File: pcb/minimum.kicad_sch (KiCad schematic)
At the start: 32 parts, among them J1 USB4155-03-C_REVA, J2 Conn_01x02, U1 RP2040, U2 SCD4x, U3 W25Q16JVUXIQ, U4 XCL220, Y1 C2E-12.000-18-1020-X-R

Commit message: routing
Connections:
- net Pi_USB_D-: now reaches R2.1, U1.46 (USB_DM)
- net Pi_USB_D+: now reaches R1.2, U1.47 (USB_DP)
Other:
- moved on the sheet: R1, R2
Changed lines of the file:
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@@
     (stroke (width 0) (type solid) (color 0 0 0 0))
   )
-  (wire (pts (xy 212.09 38.735) (xy 217.805 38.735))
-    (stroke (width 0) (type solid) (color 0 0 0 0))
-  )
-  (wire (pts (xy 212.09 41.275) (xy 217.805 41.275))
+  (wire (pts (xy 212.09 38.735) (xy 222.25 38.735))
+    (stroke (width 0) (type solid) (color 0 0 0 0))
+  )
+  (wire (pts (xy 212.09 41.275) (xy 222.25 41.275))
     (stroke (width 0) (type solid) (color 0 0 0 0))
   )
@@
     (stroke (width 0) (type solid) (color 0 0 0 0))
   )
-  (wire (pts (xy 222.885 38.735) (xy 240.665 38.735))
-    (stroke (width 0) (type solid) (color 0 0 0 0))
-  )
-  (wire (pts (xy 222.885 41.275) (xy 240.665 41.275))
+  (wire (pts (xy 227.33 38.735) (xy 240.665 38.735))
+    (stroke (width 0) (type solid) (color 0 0 0 0))
+  )
+  (wire (pts (xy 227.33 41.275) (xy 240.665 41.275))
     (stroke (width 0) (type solid) (color 0 0 0 0))
   )
@@
   )
   (label "SCL" (at 196.85 216.535 0)
+    (effects (font (size 1 1)) (justify left bottom))
+  )
+  (label "Pi_USB_D+" (at 212.725 38.735 0)
+    (effects (font (size 1 1)) (justify left bottom))
+  )
+  (label "Pi_USB_D-" (at 212.725 41.275 0)
     (effects (font (size 1 1)) (justify left bottom))
   )
@@
     (pin "2")
   )
-  (symbol (lib_id "Device:R_Small") (at 220.345 38.735 270) (unit 1)
-    (in_bom yes) (on_board yes)
-    (property "Reference" "R1" (id 0) (at 224.155 37.2068 90))
-    (property "Value" "27.4" (id 1) (at 220.345 36.8069 90))
-    (property "Footprint" "Resistor_SMD:R_0402_1005Metric" (id 2) (at 220.345 38.735 0)
-      (effects (font (size 1.27 1.27)) hide)
-    )
-    (property "Datasheet" "~" (id 3) (at 220.345 38.735 0)
+  (symbol (lib_id "Device:R_Small") (at 224.79 38.735 270) (unit 1)
+    (in_bom yes) (on_board yes)
+    (property "Reference" "R1" (id 0) (at 228.6 37.2068 90))
+    (property "Value" "27.4" (id 1) (at 224.79 36.8069 90))
+    (property "Footprint" "Resistor_SMD:R_0402_1005Metric" (id 2) (at 224.79 38.735 0)
+      (effects (font (size 1.27 1.27)) hide)
+    )
+    (property "Datasheet" "~" (id 3) (at 224.79 38.735 0)
       (effects (font (size 1.27 1.27)) hide)
     )
@@
     (pin "2")
   )
-  (symbol (lib_id "Device:R_Small") (at 220.345 41.275 90) (unit 1)
-    (in_bom yes) (on_board yes)
-    (property "Reference" "R2" (id 0) (at 224.155 42.2868 90))
-    (property "Value" "27.4" (id 1) (at 220.345 43.1569 90))
-    (property "Footprint" "Resistor_SMD:R_0402_1005Metric" (id 2) (at 220.345 41.275 0)
-      (effects (font (size 1.27 1.27)) hide)
-    )
-    (property "Datasheet" "~" (id 3) (at 220.345 41.275 0)
-      (effects (font (size 1.27 1.27)) hide)
-    )
+  (symbol (lib_id "Device:R_Small") (at 224.79 41.275 90) (unit 1)
+    (in_bom yes) (on_board yes)
+    (property "Reference" "R2" (id 0) (at 228.6 42.2868 90))
+    (property "Value" "27.4" (id 1) (at 224.79 43.1569 90))
+    (property "Footprint" "Resistor_SMD:R_0402_1005Metric" (id 2) (at 224.79 41.275 0)
+      (effects (font (size 1.27 1.27)) hide)
+    )
+    (property "Datasheet" "~" (id 3) (at 224.79 41.275 0)
+      (effects (font (size 1.27 1.27)) hide)
+    )

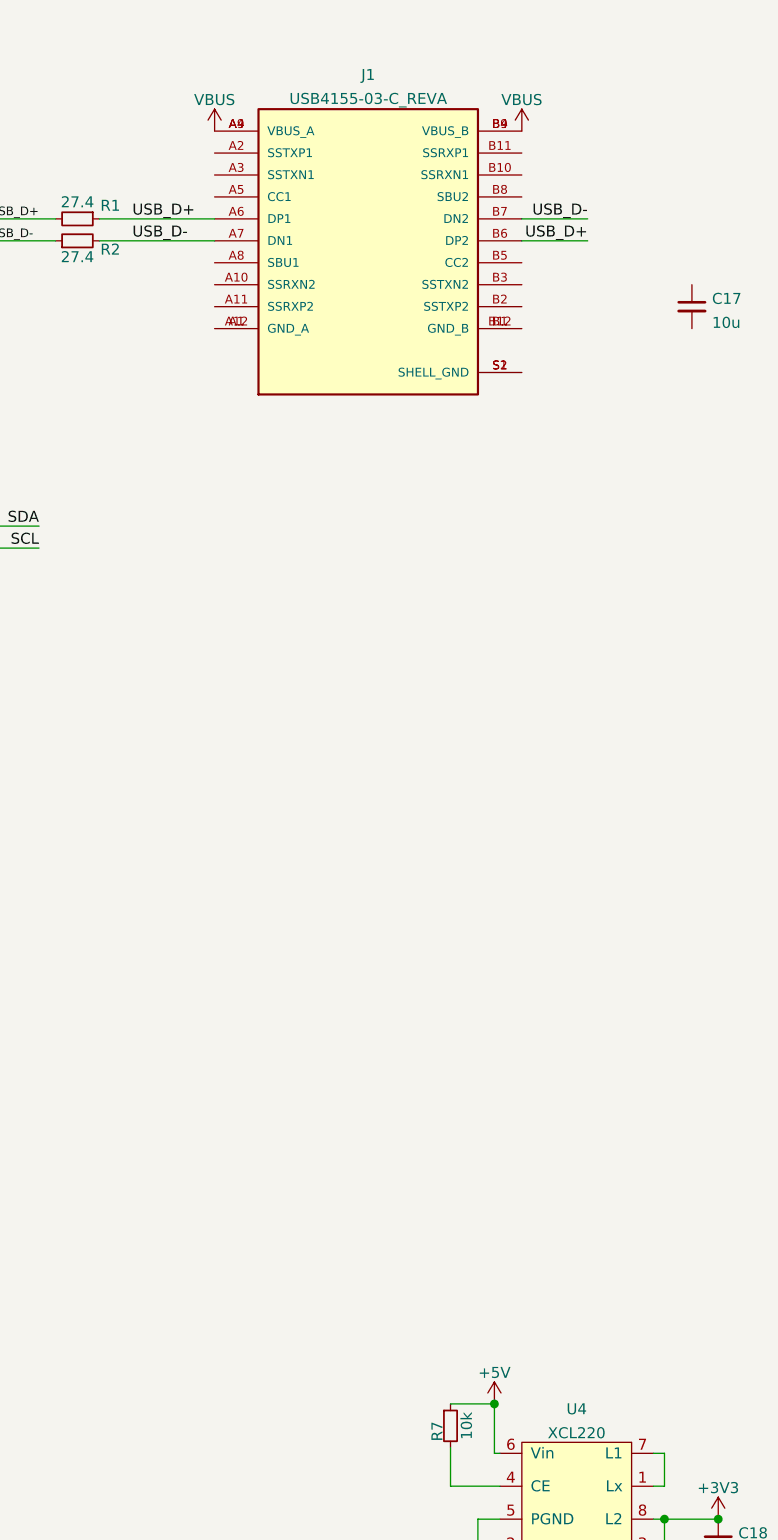
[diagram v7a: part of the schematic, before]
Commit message: routing VBUS
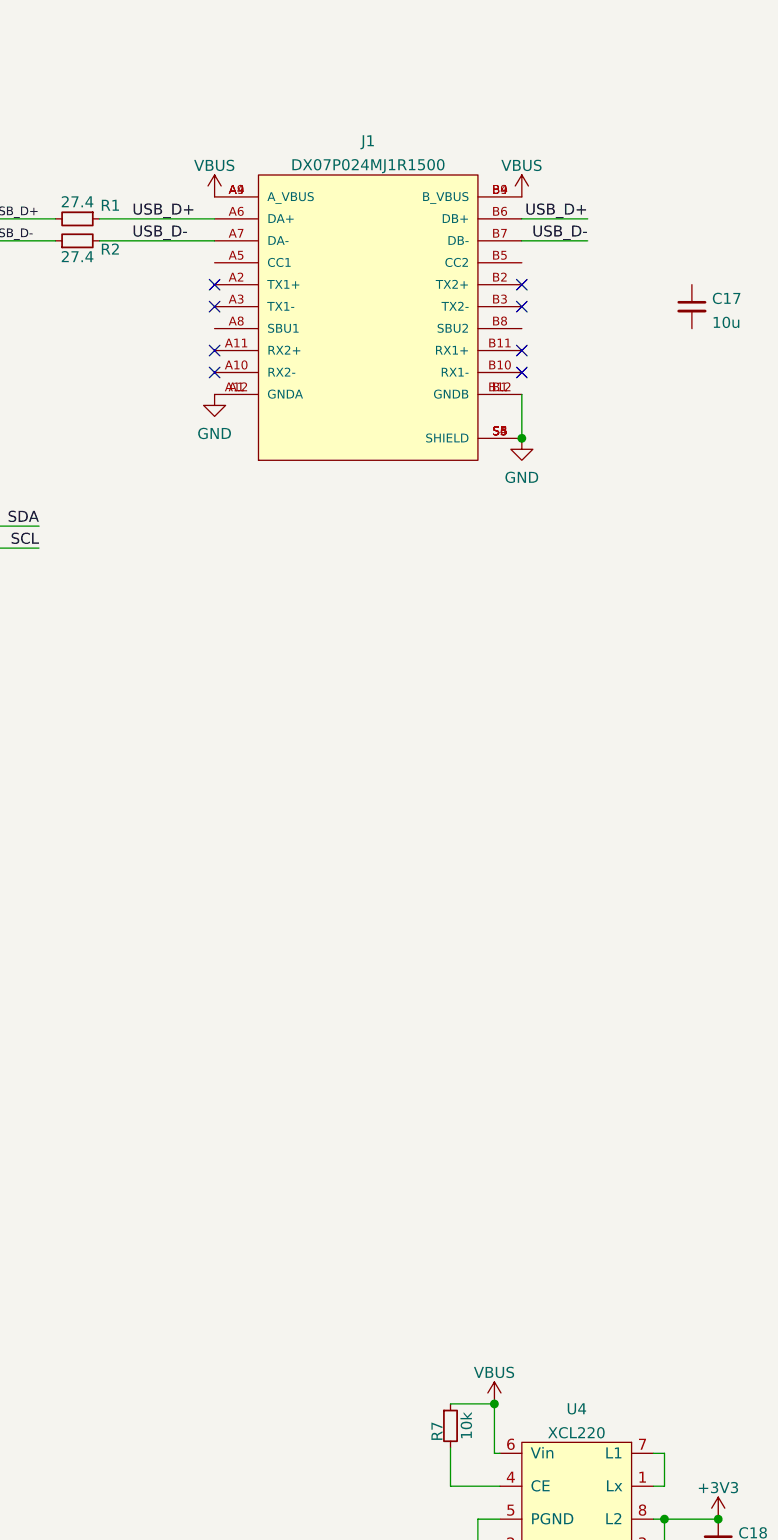
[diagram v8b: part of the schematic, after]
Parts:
- removed J1: USB4155-03-C_REVA, SMD:GCT_USB4155-03-C_REVA, symbol USB4155-03-C_REVA:USB4155-03-C_REVA
- added J1: DX07P024MJ1R1500, SMD:JAE_DX07P024MJ1R1500, symbol DX07P024MJ1R1500:DX07P024MJ1R1500
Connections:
- net +5V is gone; now on net VBUS: R7.1, U4.6 (Vin)
- net GND: now also J1.A1 (GNDA), J1.A12 (GNDA), J1.B1 (GNDB), J1.B12 (GNDB), J1.S3 (SHIELD), J1.S4 (SHIELD), J1.S5 (SHIELD), J1.S6 (SHIELD)
- net USB_D+: now also J1.A6 (DA+), J1.B6 (DB+)
- net USB_D-: now also J1.A7 (DA-), J1.B7 (DB-)
- net VBUS: now also J1.A4 (A_VBUS), J1.A9 (A_VBUS), J1.B4 (B_VBUS), J1.B9 (B_VBUS)
- no-connect marks 0 -> 8
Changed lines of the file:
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@@
   (junction (at 271.145 196.85) (diameter 1.016) (color 0 0 0 0))
   (junction (at 273.05 175.895) (diameter 1.016) (color 0 0 0 0))
+  (junction (at 276.225 64.135) (diameter 1.016) (color 0 0 0 0))
   (junction (at 292.735 189.23) (diameter 1.016) (color 0 0 0 0))
   (junction (at 298.958 189.23) (diameter 1.016) (color 0 0 0 0))
+  (no_connect (at 240.665 46.355))
+  (no_connect (at 240.665 48.895))
+  (no_connect (at 240.665 53.975))
+  (no_connect (at 240.665 56.515))
+  (no_connect (at 276.225 46.355))
+  (no_connect (at 276.225 48.895))
+  (no_connect (at 276.225 53.975))
+  (no_connect (at 276.225 56.515))
   (wire (pts (xy 17.78 45.085) (xy 27.94 45.085))
     (stroke (width 0) (type solid) (color 0 0 0 0))
@@
   )
   (wire (pts (xy 276.225 41.275) (xy 283.845 41.275))
+    (stroke (width 0) (type solid) (color 0 0 0 0))
+  )
+  (wire (pts (xy 276.225 59.055) (xy 276.225 64.135))
     (stroke (width 0) (type solid) (color 0 0 0 0))
   )
@@
     (effects (font (size 1.27 1.27)) (justify left bottom))
   )
-  (label "USB_D-" (at 283.845 38.735 180)
+  (label "USB_D+" (at 283.845 38.735 180)
     (effects (font (size 1.27 1.27)) (justify right bottom))
   )
-  (label "USB_D+" (at 283.845 41.275 180)
+  (label "USB_D-" (at 283.845 41.275 180)
     (effects (font (size 1.27 1.27)) (justify right bottom))
   )
@@
     (pin "1")
   )
-  (symbol (lib_id "power:VBUS") (at 240.665 28.575 0) (unit 1)
-    (in_bom yes) (on_board yes) (fields_autoplaced)
-    (property "Reference" "#PWR0123" (id 0) (at 240.665 32.385 0)
-      (effects (font (size 1.27 1.27)) hide)
-    )
-    (property "Value" "VBUS" (id 1) (at 240.665 24.9704 0))
-    (property "Footprint" "" (id 2) (at 240.665 28.575 0)
-      (effects (font (size 1.27 1.27)) hide)
-    )
-    (property "Datasheet" "" (id 3) (at 240.665 28.575 0)
-      (effects (font (size 1.27 1.27)) hide)
-    )
-    (pin "1")
-  )
-  (symbol (lib_id "power:+5V") (at 273.05 175.895 0) (unit 1)
+  (symbol (lib_id "power:VBUS") (at 240.665 36.195 0) (unit 1)
     (in_bom yes) (on_board yes)
-    (property "Reference" "#PWR0127" (id 0) (at 273.05 179.705 0)
-      (effects (font (size 1.27 1.27)) hide)
-    )
-    (property "Value" "+5V" (id 1) (at 273.05 172.2904 0))
+    (property "Reference" "#PWR0123" (id 0) (at 240.665 40.005 0)
+      (effects (font (size 1.27 1.27)) hide)
+    )
+    (property "Value" "VBUS" (id 1) (at 240.665 32.5904 0))
+    (property "Footprint" "" (id 2) (at 240.665 36.195 0)
+      (effects (font (size 1.27 1.27)) hide)
+    )
+    (property "Datasheet" "" (id 3) (at 240.665 36.195 0)
+      (effects (font (size 1.27 1.27)) hide)
+    )
+    (pin "1")
+  )
+  (symbol (lib_id "power:VBUS") (at 273.05 175.895 0) (unit 1)
+    (in_bom yes) (on_board yes) (fields_autoplaced)
+    (property "Reference" "#PWR?" (id 0) (at 273.05 179.705 0)
+      (effects (font (size 1.27 1.27)) hide)
+    )
+    (property "Value" "VBUS" (id 1) (at 273.05 172.2904 0))
     (property "Footprint" "" (id 2) (at 273.05 175.895 0)
       (effects (font (size 1.27 1.27)) hide)
@@
     (pin "1")
   )
-  (symbol (lib_id "power:VBUS") (at 276.225 28.575 0) (unit 1)
-    (in_bom yes) (on_board yes) (fields_autoplaced)
-    (property "Reference" "#PWR0122" (id 0) (at 276.225 32.385 0)
-      (effects (font (size 1.27 1.27)) hide)
-    )
-    (property "Value" "VBUS" (id 1) (at 276.225 24.9704 0))
-    (property "Footprint" "" (id 2) (at 276.225 28.575 0)
-      (effects (font (size 1.27 1.27)) hide)
-    )
-    (property "Datasheet" "" (id 3) (at 276.225 28.575 0)
+  (symbol (lib_id "power:VBUS") (at 276.225 36.195 0) (unit 1)
+    (in_bom yes) (on_board yes) (fields_autoplaced)
+    (property "Reference" "#PWR0122" (id 0) (at 276.225 40.005 0)
+      (effects (font (size 1.27 1.27)) hide)
+    )
+    (property "Value" "VBUS" (id 1) (at 276.225 32.5904 0))
+    (property "Footprint" "" (id 2) (at 276.225 36.195 0)
+      (effects (font (size 1.27 1.27)) hide)
+    )
+    (property "Datasheet" "" (id 3) (at 276.225 36.195 0)
       (effects (font (size 1.27 1.27)) hide)
     )
@@
     (pin "1")
   )
+  (symbol (lib_id "power:GND") (at 240.665 59.055 0) (unit 1)
+    (in_bom yes) (on_board yes) (fields_autoplaced)
+    (property "Reference" "#PWR0132" (id 0) (at 240.665 65.405 0)
+      (effects (font (size 1.27 1.27)) hide)
+    )
+    (property "Value" "GND" (id 1) (at 240.665 63.6176 0))
+    (property "Footprint" "" (id 2) (at 240.665 59.055 0)
+      (effects (font (size 1.27 1.27)) hide)
+    )
+    (property "Datasheet" "" (id 3) (at 240.665 59.055 0)
+      (effects (font (size 1.27 1.27)) hide)
+    )
+    (pin "1")
+  )
   (symbol (lib_id "power:GND") (at 271.145 198.755 0) (unit 1)
     (in_bom yes) (on_board yes) (fields_autoplaced)
@@
     )
     (property "Datasheet" "" (id 3) (at 271.145 198.755 0)
+      (effects (font (size 1.27 1.27)) hide)
+    )
+    (pin "1")
+  )
+  (symbol (lib_id "power:GND") (at 276.225 64.135 0) (unit 1)
+    (in_bom yes) (on_board yes) (fields_autoplaced)
+    (property "Reference" "#PWR0131" (id 0) (at 276.225 70.485 0)
+      (effects (font (size 1.27 1.27)) hide)
+    )
+    (property "Value" "GND" (id 1) (at 276.225 68.6976 0))
+    (property "Footprint" "" (id 2) (at 276.225 64.135 0)
+      (effects (font (size 1.27 1.27)) hide)
+    )
+    (property "Datasheet" "" (id 3) (at 276.225 64.135 0)
       (effects (font (size 1.27 1.27)) hide)
     )
@@
     (pin "9")
   )
-  (symbol (lib_id "USB4155-03-C_REVA:USB4155-03-C_REVA") (at 258.445 41.275 0) (unit 1)
-    (in_bom yes) (on_board yes) (fields_autoplaced)
-    (property "Reference" "J1" (id 0) (at 258.445 22.0684 0))
-    (property "Value" "USB4155-03-C_REVA" (id 1) (at 258.445 24.8435 0))
-    (property "Footprint" "SMD:GCT_USB4155-03-C_REVA" (id 2) (at 258.445 41.275 0)
+  (symbol (lib_id "DX07P024MJ1R1500:DX07P024MJ1R1500") (at 258.445 51.435 0) (unit 1)
+    (in_bom yes) (on_board yes) (fields_autoplaced)
+    (property "Reference" "J1" (id 0) (at 258.445 29.7392 0))
+    (property "Value" "DX07P024MJ1R1500" (id 1) (at 258.445 32.5143 0))
+    (property "Footprint" "SMD:JAE_DX07P024MJ1R1500" (id 2) (at 258.445 51.435 0)
       (effects (font (size 1.27 1.27)) (justify left bottom) hide)
     )
-    (property "Datasheet" "" (id 3) (at 258.445 41.275 0)
+    (property "Datasheet" "" (id 3) (at 258.445 51.435 0)
       (effects (font (size 1.27 1.27)) (justify left bottom) hide)
     )
-    (property "MANUFACTURER" "GCT" (id 4) (at 258.445 41.275 0)
+    (property "MAXIMUM_PACKAGE_HEIGHT" "1.625mm" (id 4) (at 258.445 51.435 0)
       (effects (font (size 1.27 1.27)) (justify left bottom) hide)
     )
-    (property "MAXIMUM_PACKAGE_HEIGHT" "2.9 mm" (id 5) (at 258.445 41.275 0)
+    (property "PARTREV" "1.0" (id 5) (at 258.445 51.435 0)
       (effects (font (size 1.27 1.27)) (justify left bottom) hide)
     )
-    (property "PARTREV" "A" (id 6) (at 258.445 41.275 0)
+    (property "MANUFACTURER" "JAE Electronics" (id 6) (at 258.445 51.435 0)
       (effects (font (size 1.27 1.27)) (justify left bottom) hide)
     )
-    (property "STANDARD" "Manufacturer Recommendations" (id 7) (at 258.445 41.275 0)
+    (property "STANDARD" "Manufacturer Recommendations" (id 7) (at 258.445 51.435 0)
       (effects (font (size 1.27 1.27)) (justify left bottom) hide)
     )
@@
     (pin "B8")
     (pin "B9")
-    (pin "S1")
-    (pin "S2")
+    (pin "S3")
+    (pin "S4")
+    (pin "S5")
+    (pin "S6")
   )
   (symbol (lib_id "W25Q128:W25Q128JVPIM") (at 95.25 223.52 0) (unit 1)
@@
       (reference "#PWR0126") (unit 1) (value "+3V3") (footprint "")
     )
-    (path "/adff1247-fa95-4dad-be61-d7b6b9d309d7"
-      (reference "#PWR0127") (unit 1) (value "+5V") (footprint "")
-    )
     (path "/6f6d4540-ef37-47a0-98e2-40a1cdda8c1c"
       (reference "#PWR0128") (unit 1) (value "GND") (footprint "")
@@
       (reference "#PWR0130") (unit 1) (value "GND") (footprint "")
     )
+    (path "/ee7a92bb-faae-4c5b-9ef6-537f906134b2"
+      (reference "#PWR0131") (unit 1) (value "GND") (footprint "")
+    )
+    (path "/a55ea6c4-2e87-4cc8-ba84-8ef126feace6"
+      (reference "#PWR0132") (unit 1) (value "GND") (footprint "")
+    )
+    (path "/fbe7173c-3624-4a8e-9ddc-41f9ad3603b0"
+      (reference "#PWR?") (unit 1) (value "VBUS") (footprint "")
+    )
     (path "/e7effd1f-dcf0-44f9-acf3-2bc5919ae9df"
       (reference "C1") (unit 1) (value "100n") (footprint "Capacitor_SMD:C_0402_1005Metric")
@@
       (reference "C18") (unit 1) (value "10u") (footprint "Capacitor_SMD:C_0603_1608Metric")
     )
-    (path "/aa5fbedd-971e-40bd-9acd-9e69b3a25ae2"
-      (reference "J1") (unit 1) (value "USB4155-03-C_REVA") (footprint "SMD:GCT_USB4155-03-C_REVA")
+    (path "/055c229d-49d0-4802-a7e2-2793179f3436"
+      (reference "J1") (unit 1) (value "DX07P024MJ1R1500") (footprint "SMD:JAE_DX07P024MJ1R1500")
     )
     (path "/91fc2ebd-191c-45d0-9219-b62ff489e8df"
